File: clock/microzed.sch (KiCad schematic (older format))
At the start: 12 parts, among them U401 74LVC541

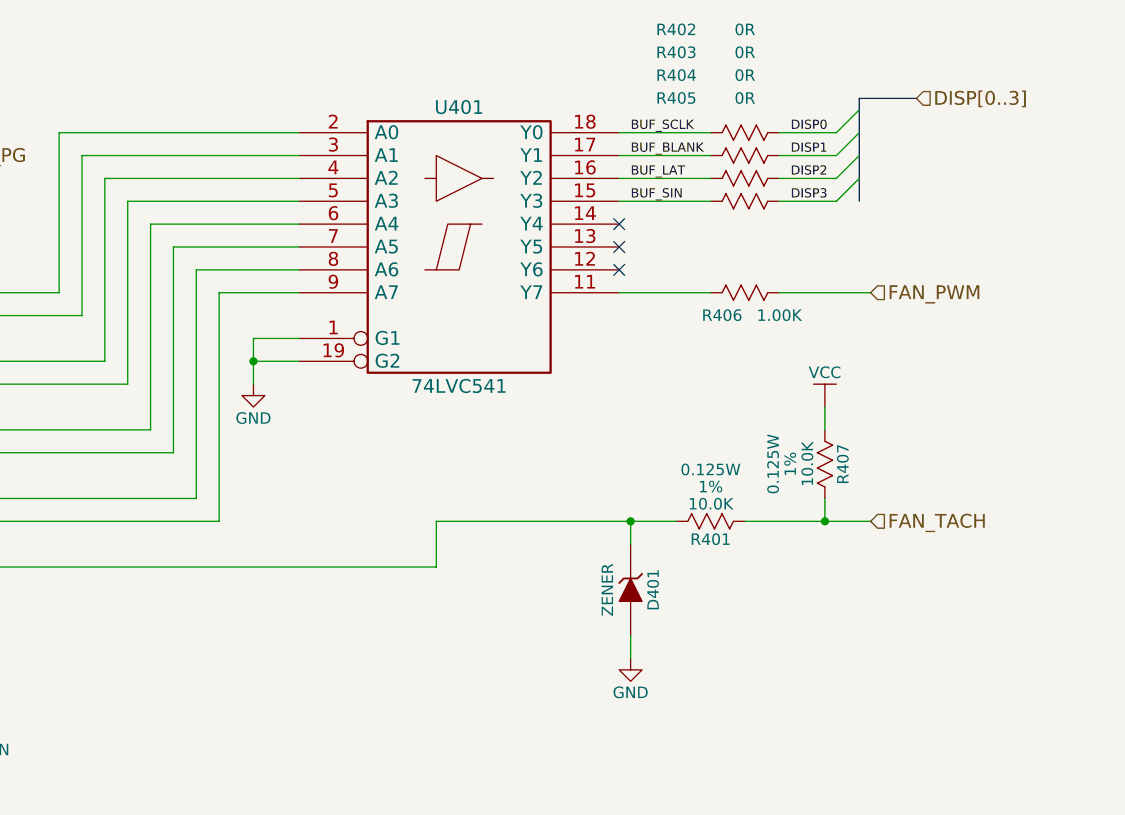
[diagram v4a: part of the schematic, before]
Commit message: Add net names to most of the nets.
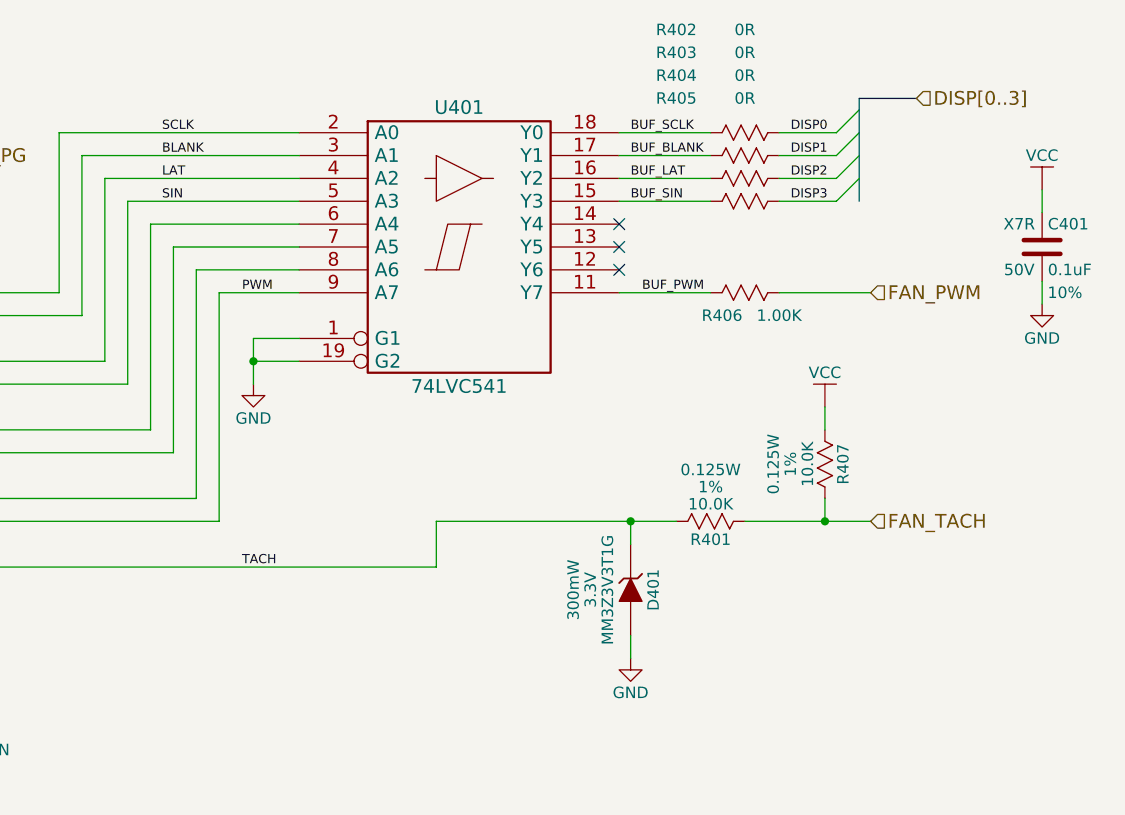
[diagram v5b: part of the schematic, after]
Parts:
- added C401: 0.1uF, Capacitors_SMD:C_0805_HandSoldering, symbol C
- D401: value ZENER -> MM3Z3V3T1G; footprint Diodes_SMD:SOD-123 -> Diodes_SMD:SOD-323; Manufacturer (none) -> ON Semiconductor; PartNum (none) -> MM3Z3V3T1G; Power (none) -> 300mW; Voltage (none) -> 3.3V
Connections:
- net GND: now also C401.2
- net VCC: now also C401.1
- net SCLK: now reaches PX1.17, U401.2 (A0)
- net BLANK: now reaches PX1.19, U401.3 (A1)
- net LAT: now reaches PX1.23, U401.4 (A2)
- net SIN: now reaches PX1.25, U401.5 (A3)
- net PWM: now reaches PX1.37, U401.9 (A7)
- net TACH: now reaches D401.1 (K), PX1.41, R401.2
- net BUF_PWM: now reaches R406.2, U401.11 (Y7)
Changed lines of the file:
@@
 P 9150 3350
 F 0 "D401" H 9150 3450 50  0000 C CNN
-F 1 "ZENER" H 9150 3250 50  0000 C CNN
-F 2 "Diodes_SMD:SOD-123" H 9150 3350 60  0001 C CNN
+F 1 "MM3Z3V3T1G" H 9150 3250 50  0000 C CNN
+F 2 "Diodes_SMD:SOD-323" H 9150 3350 60  0001 C CNN
 F 3 "" H 9150 3350 60  0000 C CNN
+F 4 "3.3V" H 9150 3175 50  0000 C CNN "Voltage"
+F 5 "300mW" H 9150 3100 50  0000 C CNN "Power"
+F 6 "ON Semiconductor" H 9150 3350 50  0001 C CNN "Manufacturer"
+F 7 "MM3Z3V3T1G" H 9150 3350 50  0001 C CNN "PartNum"
 	1    9150 3350
 	0    1    1    0
@@
 	1    0    0    -1
 $EndComp
+Text Label 7100 1350 0    40   ~ 0
+SCLK
+Text Label 7100 1450 0    40   ~ 0
+BLANK
+Text Label 7100 1550 0    40   ~ 0
+LAT
+Text Label 7100 1650 0    40   ~ 0
+SIN
+Text Label 7450 2050 0    40   ~ 0
+PWM
+Text Label 9200 2050 0    40   ~ 0
+BUF_PWM
+Text Label 7450 3250 0    40   ~ 0
+TACH
+$Comp
+L GND #PWR072
+U 1 1 56403C33
+P 10950 2100
+F 0 "#PWR072" H 10950 1850 50  0001 C CNN
+F 1 "GND" H 10950 1950 50  0000 C CNN
+F 2 "" H 10950 2100 60  0000 C CNN
+F 3 "" H 10950 2100 60  0000 C CNN
+	1    10950 2100
+	1    0    0    -1
+$EndComp
+Wire Wire Line
+	10950 2000 10950 2100
+Wire Wire Line
+	10950 1700 10950 1600
+$Comp
+L C C401
+U 1 1 56403C40
+P 10950 1850
+F 0 "C401" H 10975 1950 50  0000 L CNN
+F 1 "0.1uF" H 10975 1750 50  0000 L CNN
+F 2 "Capacitors_SMD:C_0805_HandSoldering" H 10988 1700 30  0001 C CNN
+F 3 "" H 10950 1850 60  0000 C CNN
+F 4 "50V" H 10850 1750 50  0000 C CNN "Voltage"
+F 5 "10%" H 11050 1650 50  0000 C CNN "Tolerance"
+F 6 "X7R" H 10850 1950 50  0000 C CNN "Dielectric"
+F 7 "Kemet" H 10950 1850 50  0001 C CNN "Manufacturer"
+F 8 "C0805C104K5RACTU" H 10950 1850 50  0001 C CNN "PartNum"
+	1    10950 1850
+	1    0    0    -1
+$EndComp
+$Comp
+L VCC #PWR073
+U 1 1 56403C47
+P 10950 1600
+F 0 "#PWR073" H 10950 1450 50  0001 C CNN
+F 1 "VCC" H 10950 1750 50  0000 C CNN
+F 2 "" H 10950 1600 60  0000 C CNN
+F 3 "" H 10950 1600 60  0000 C CNN
+	1    10950 1600
+	1    0    0    -1
+$EndComp

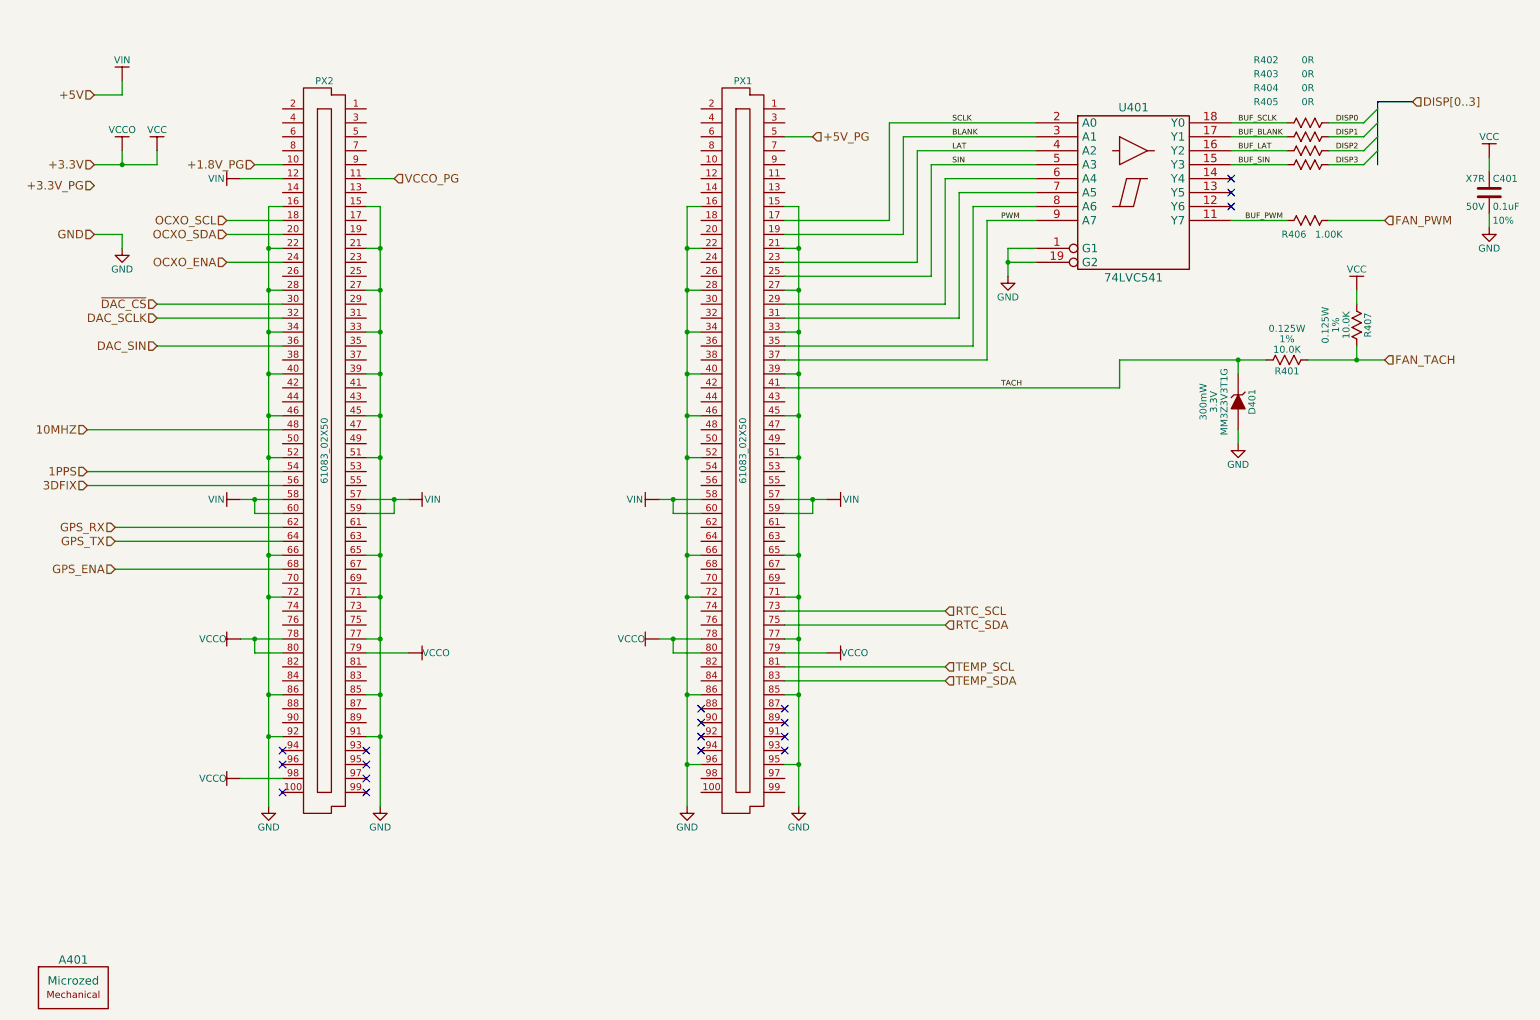
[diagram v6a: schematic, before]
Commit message: Clean up most of the schematic DRC errors. Update placement.
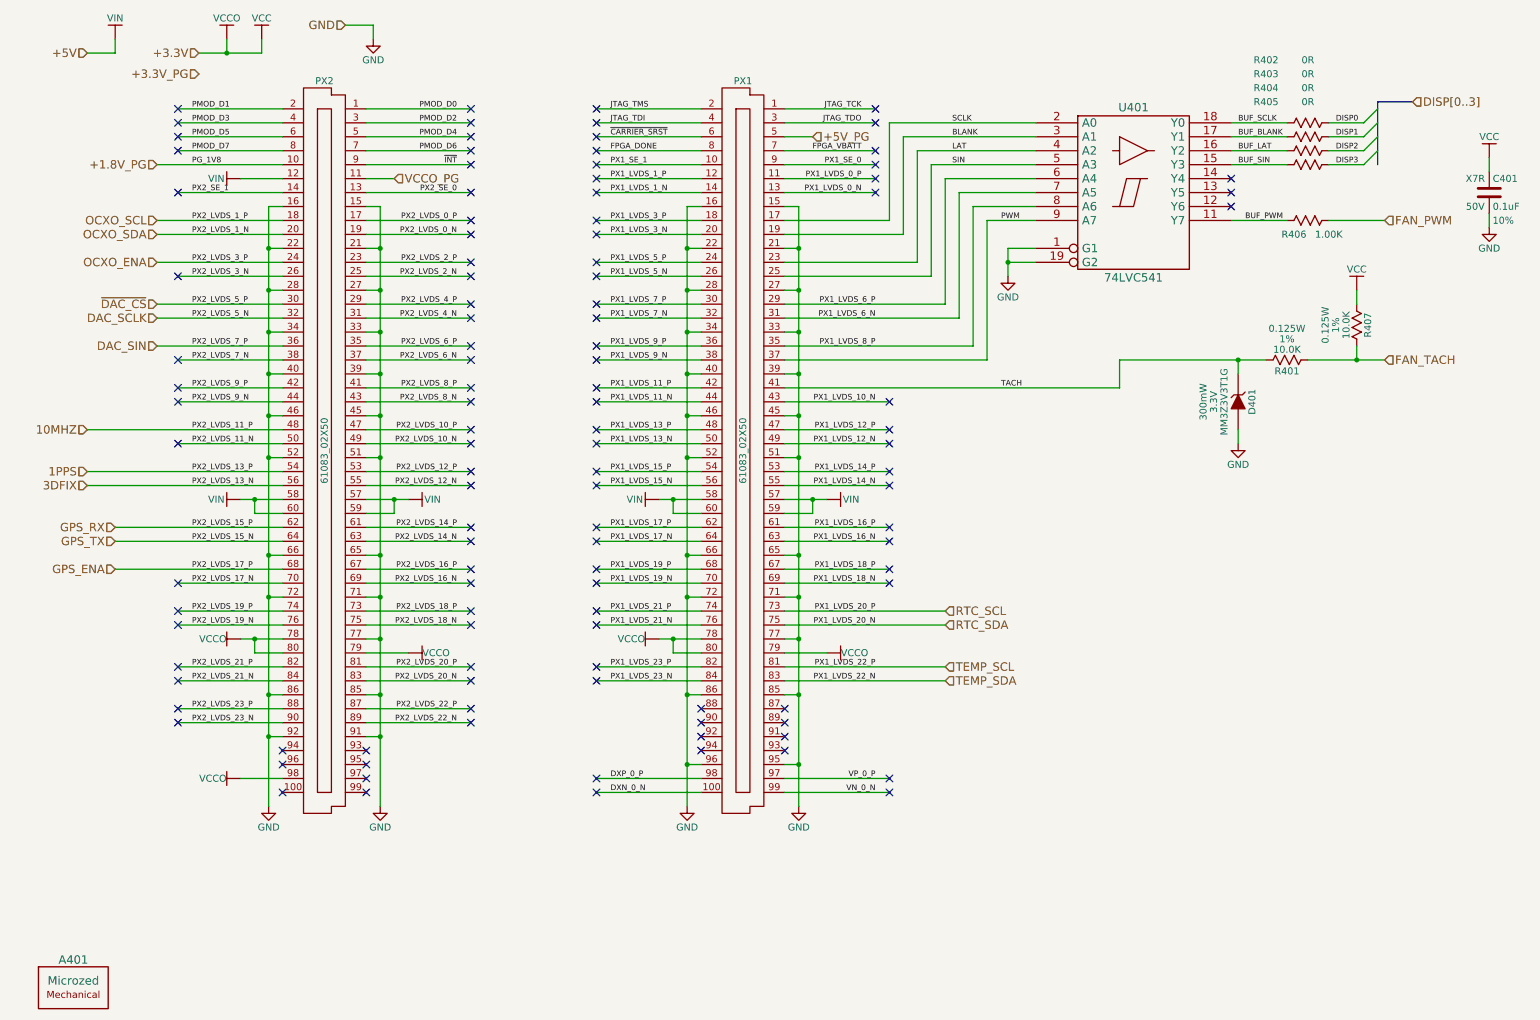
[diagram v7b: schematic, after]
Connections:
- net PMOD_D0: now reaches PX2.1
- net PX2_SE_0: now reaches PX2.13
- net PX2_SE_1: now reaches PX2.14
- net PX2_LVDS_0_P: now reaches PX2.17
- net PX2_LVDS_0_N: now reaches PX2.19
- net PMOD_D1: now reaches PX2.2
- net PX2_LVDS_2_P: now reaches PX2.23
- net PX2_LVDS_2_N: now reaches PX2.25
- net PX2_LVDS_3_N: now reaches PX2.26
- net PX2_LVDS_4_P: now reaches PX2.29
- net PMOD_D2: now reaches PX2.3
- net PX2_LVDS_4_N: now reaches PX2.31
- net PX2_LVDS_6_P: now reaches PX2.35
- net PX2_LVDS_6_N: now reaches PX2.37
- net PX2_LVDS_7_N: now reaches PX2.38
- net PMOD_D3: now reaches PX2.4
- net PX2_LVDS_8_P: now reaches PX2.41
- net PX2_LVDS_9_P: now reaches PX2.42
- net PX2_LVDS_8_N: now reaches PX2.43
- net PX2_LVDS_9_N: now reaches PX2.44
- net PX2_LVDS_10_P: now reaches PX2.47
- net PX2_LVDS_10_N: now reaches PX2.49
- net PMOD_D4: now reaches PX2.5
- net PX2_LVDS_11_N: now reaches PX2.50
- net PX2_LVDS_12_P: now reaches PX2.53
- net PX2_LVDS_12_N: now reaches PX2.55
- net PMOD_D5: now reaches PX2.6
- net PX2_LVDS_14_P: now reaches PX2.61
- net PX2_LVDS_14_N: now reaches PX2.63
- net PX2_LVDS_16_P: now reaches PX2.67
- net PX2_LVDS_16_N: now reaches PX2.69
- net PMOD_D6: now reaches PX2.7
- net PX2_LVDS_17_N: now reaches PX2.70
- net PX2_LVDS_18_P: now reaches PX2.73
- net PX2_LVDS_19_P: now reaches PX2.74
- net PX2_LVDS_18_N: now reaches PX2.75
- net PX2_LVDS_19_N: now reaches PX2.76
- net PMOD_D7: now reaches PX2.8
- net PX2_LVDS_20_P: now reaches PX2.81
- net PX2_LVDS_21_P: now reaches PX2.82
- net PX2_LVDS_20_N: now reaches PX2.83
- net PX2_LVDS_21_N: now reaches PX2.84
- net PX2_LVDS_22_P: now reaches PX2.87
- net PX2_LVDS_23_P: now reaches PX2.88
- net PX2_LVDS_22_N: now reaches PX2.89
- net ~INT~: now reaches PX2.9
- net PX2_LVDS_23_N: now reaches PX2.90
- net JTAG_TCK: now reaches PX1.1
- net PX1_SE_1: now reaches PX1.10
- net DXN_0_N: now reaches PX1.100
- net PX1_LVDS_0_P: now reaches PX1.11
- net PX1_LVDS_1_P: now reaches PX1.12
- net PX1_LVDS_0_N: now reaches PX1.13
- net PX1_LVDS_1_N: now reaches PX1.14
- net PX1_LVDS_3_P: now reaches PX1.18
- net JTAG_TMS: now reaches PX1.2
- net PX1_LVDS_3_N: now reaches PX1.20
- net PX1_LVDS_5_P: now reaches PX1.24
- net PX1_LVDS_5_N: now reaches PX1.26
- net PX1_LVDS_6_P: now reaches PX1.29, U401.6 (A4)
- net JTAG_TDO: now reaches PX1.3
- net PX1_LVDS_7_P: now reaches PX1.30
- net PX1_LVDS_6_N: now reaches PX1.31, U401.7 (A5)
- net PX1_LVDS_7_N: now reaches PX1.32
- net PX1_LVDS_8_P: now reaches PX1.35, U401.8 (A6)
- net PX1_LVDS_9_P: now reaches PX1.36
- net PX1_LVDS_9_N: now reaches PX1.38
- net JTAG_TDI: now reaches PX1.4
- net PX1_LVDS_11_P: now reaches PX1.42
- net PX1_LVDS_10_N: now reaches PX1.43
- net PX1_LVDS_11_N: now reaches PX1.44
- net PX1_LVDS_12_P: now reaches PX1.47
- net PX1_LVDS_13_P: now reaches PX1.48
- net PX1_LVDS_12_N: now reaches PX1.49
- net PX1_LVDS_13_N: now reaches PX1.50
- net PX1_LVDS_14_P: now reaches PX1.53
- net PX1_LVDS_15_P: now reaches PX1.54
- net PX1_LVDS_14_N: now reaches PX1.55
- net PX1_LVDS_15_N: now reaches PX1.56
- net ~CARRIER_SRST~: now reaches PX1.6
- net PX1_LVDS_16_P: now reaches PX1.61
- net PX1_LVDS_17_P: now reaches PX1.62
- net PX1_LVDS_16_N: now reaches PX1.63
- net PX1_LVDS_17_N: now reaches PX1.64
- net PX1_LVDS_18_P: now reaches PX1.67
- net PX1_LVDS_19_P: now reaches PX1.68
- net PX1_LVDS_18_N: now reaches PX1.69
- net FPGA_VBATT: now reaches PX1.7
- net PX1_LVDS_19_N: now reaches PX1.70
- net PX1_LVDS_21_P: now reaches PX1.74
- net PX1_LVDS_21_N: now reaches PX1.76
- net FPGA_DONE: now reaches PX1.8
- net PX1_LVDS_23_P: now reaches PX1.82
- net PX1_LVDS_23_N: now reaches PX1.84
- net PX1_SE_0: now reaches PX1.9
- net VP_0_P: now reaches PX1.97
- net DXP_0_P: now reaches PX1.98
- net VN_0_N: now reaches PX1.99
- no-connect marks 18 -> 113

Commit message: Checkpoint PCB.
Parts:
- D401: footprint Diodes_SMD:SOD-323 -> local:SOD-323_477-02-H
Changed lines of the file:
@@
 F 0 "D401" H 9150 3450 50  0000 C CNN
 F 1 "MM3Z3V3T1G" H 9150 3250 50  0000 C CNN
-F 2 "Diodes_SMD:SOD-323" H 9150 3350 60  0001 C CNN
+F 2 "local:SOD-323_477-02-H" H 9150 3350 60  0001 C CNN
 F 3 "" H 9150 3350 60  0000 C CNN
 F 4 "3.3V" H 9150 3175 50  0000 C CNN "Voltage"
